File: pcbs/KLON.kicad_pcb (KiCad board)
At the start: 2 copper layers, 159.6 x 117.7 mm, 67 parts

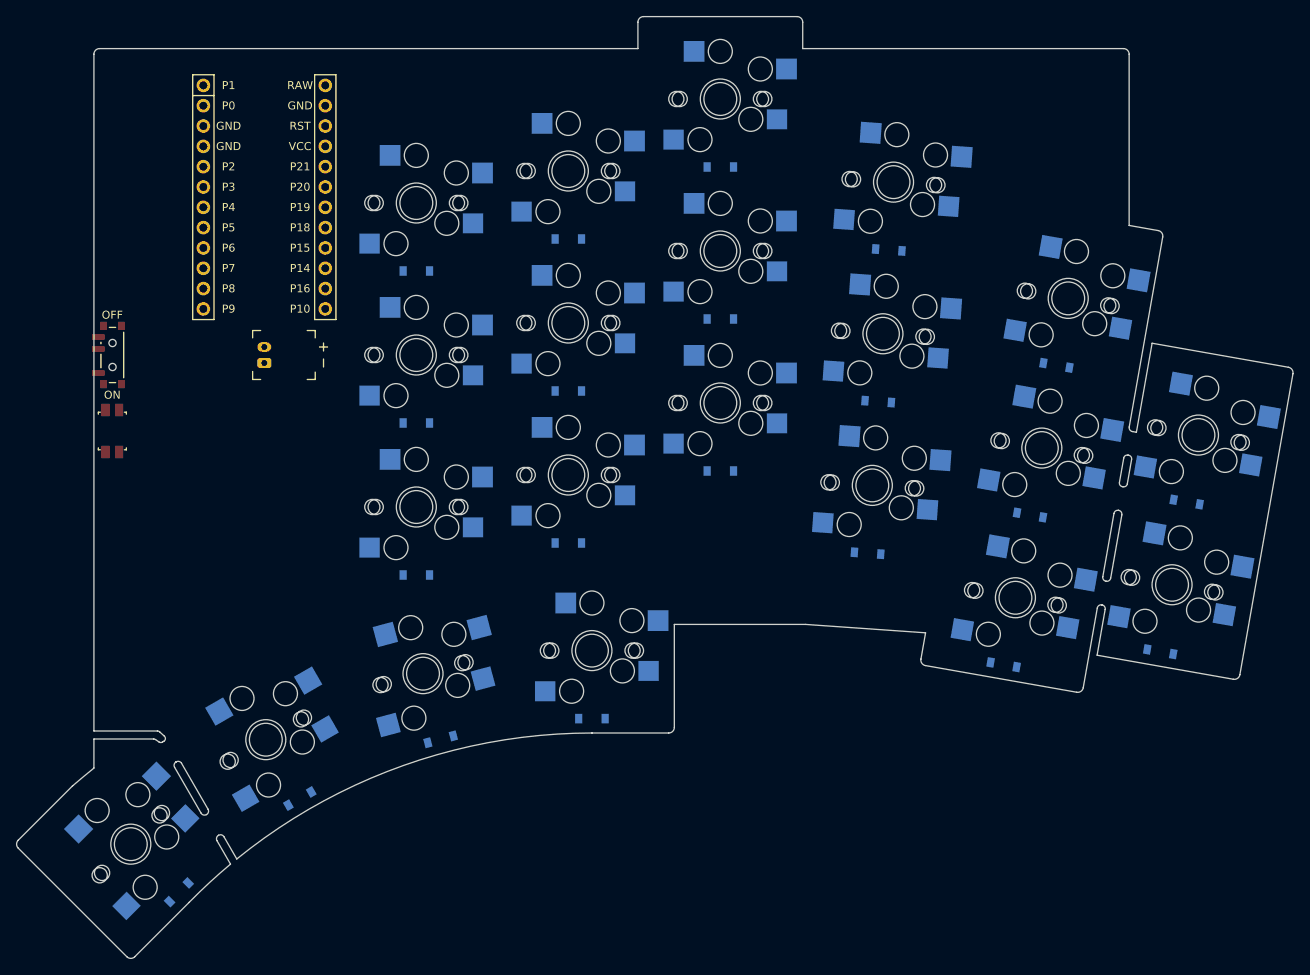
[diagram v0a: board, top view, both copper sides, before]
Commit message: updated config.yaml ; moved reset, rotary, and created ttrs
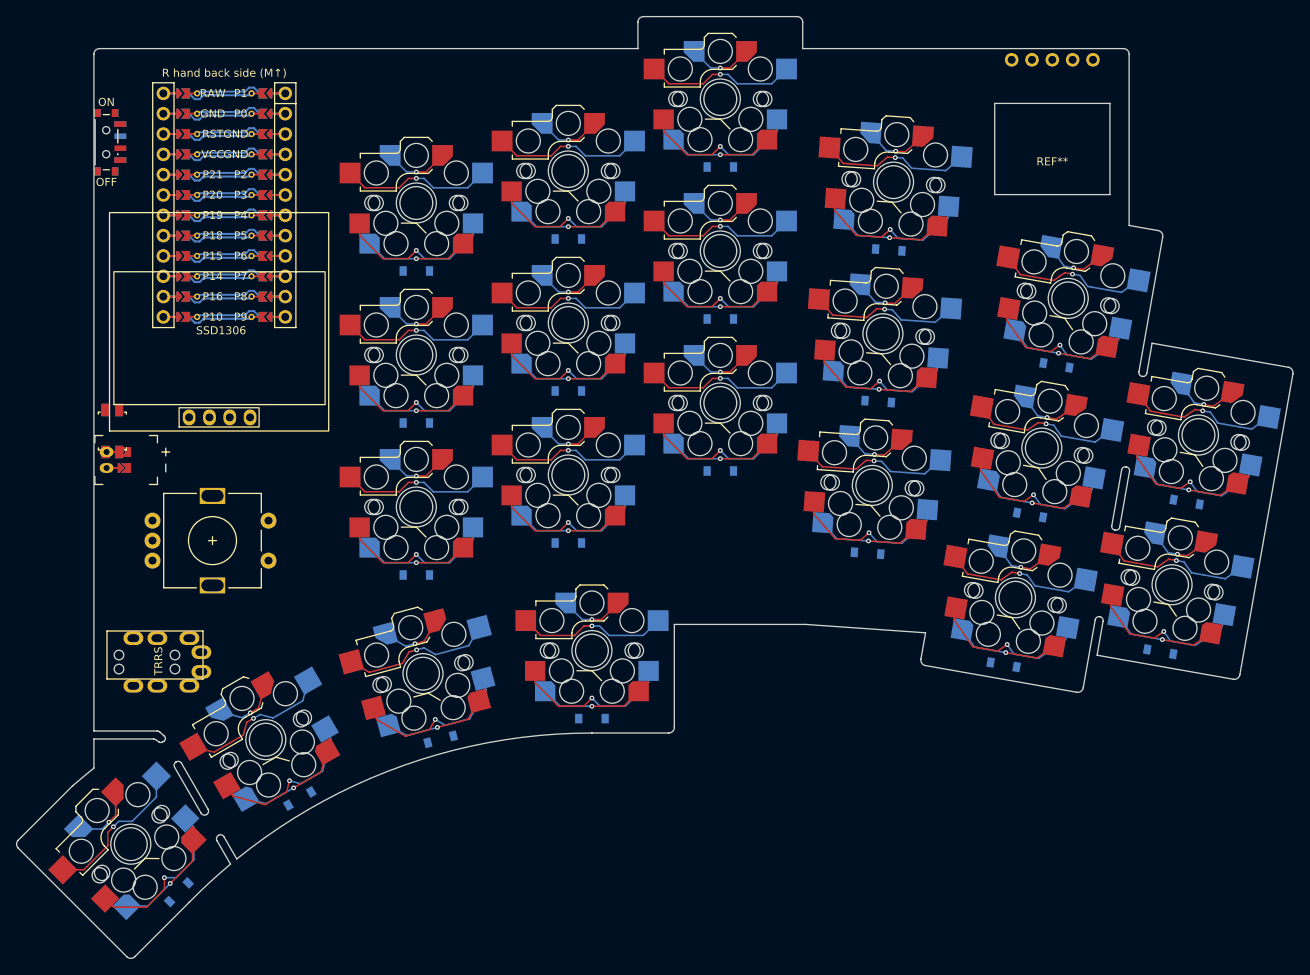
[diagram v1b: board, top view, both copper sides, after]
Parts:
- added XX1: , Pimoroni Haptic Buzz DRV2605L Driver, F.Cu at (249.5, 104.5)
- added XX2: , RotaryEncoder_Alps_EC11E-Switch_Vertical_H20mm-keebio_modified, F.Cu at (144.5, 154.2)
- added XX3: , SSD1306_128x64OLED, F.Cu at (145.6, 128.2)
- added XX4: , MJ-4PP-9, F.Cu at (131.3, 168.5)
- moved PWR1 26.6 mm to (131.3, 104.4), turned to 180 degrees
- moved JST1 23.7 mm to (131.3, 144.1)
- moved MCU1 5.10 mm to (146.0, 111.0)
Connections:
- JST1 pad 1: GND -> BAT_P
- JST1 pad 2: BAT_P -> GND
- MCU1 pad 1: RAW -> MCU1_1
- MCU1 pad 10: P14 -> MCU1_10
- MCU1 pad 11: P16 -> MCU1_11
- MCU1 pad 12: P10 -> MCU1_12
- MCU1 pad 13: P9 -> MCU1_13
- MCU1 pad 14: P8 -> MCU1_14
- MCU1 pad 15: P7 -> MCU1_15
- MCU1 pad 16: P6 -> MCU1_16
- MCU1 pad 17: P5 -> MCU1_17
- MCU1 pad 18: P4 -> MCU1_18
- MCU1 pad 19: P3 -> MCU1_19
- MCU1 pad 2: GND -> MCU1_2
- MCU1 pad 20: P2 -> MCU1_20
- MCU1 pad 21: GND -> MCU1_21
- MCU1 pad 22: GND -> MCU1_22
- MCU1 pad 23: P0 -> MCU1_23
- MCU1 pad 24: P1 -> MCU1_24
- MCU1 pad 3: RST -> MCU1_3
- MCU1 pad 4: VCC -> MCU1_4
- MCU1 pad 5: P21 -> MCU1_5
- MCU1 pad 6: P20 -> MCU1_6
- MCU1 pad 7: P19 -> MCU1_7
- MCU1 pad 8: P18 -> MCU1_8
- MCU1 pad 9: P15 -> MCU1_9
- PWR1 pad 3: (no net) -> BAT_P
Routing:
- net (no net): track 0.00 -> 733.6 mm, vias 0 -> 42
- net 3_r0: track 0.00 -> 42.2 mm, vias 0 -> 2
- net inner_home: track 0.00 -> 42.2 mm, vias 0 -> 2
- net middle_bottom: track 0.00 -> 42.2 mm, vias 0 -> 2
- net inner_bottom: track 0.00 -> 42.2 mm, vias 0 -> 2
- net index_bottom: track 0.00 -> 42.2 mm, vias 0 -> 2
- net 1_r0: track 0.00 -> 42.2 mm, vias 0 -> 2
- net index_home: track 0.00 -> 42.2 mm, vias 0 -> 2
- net middle_top: track 0.00 -> 42.2 mm, vias 0 -> 2
- net middle_home: track 0.00 -> 42.2 mm, vias 0 -> 2
- net inner_top: track 0.00 -> 42.2 mm, vias 0 -> 2
- net index_top: track 0.00 -> 42.2 mm, vias 0 -> 2
- net ring_bottom: track 0.00 -> 42.2 mm, vias 0 -> 2
- net ring_top: track 0.00 -> 42.2 mm, vias 0 -> 2
- net ring_home: track 0.00 -> 42.2 mm, vias 0 -> 2
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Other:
- outline, holes or cut-outs redrawn
